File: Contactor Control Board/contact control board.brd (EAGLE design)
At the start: 75.9 x 50.8 mm, 29 parts, among them K1 DS2Y-S-DC5V, Q1 2n2222, Q3 2n2222, Q4 MOSFET-NCHANNELFQP30N06L, U1 LM393AN

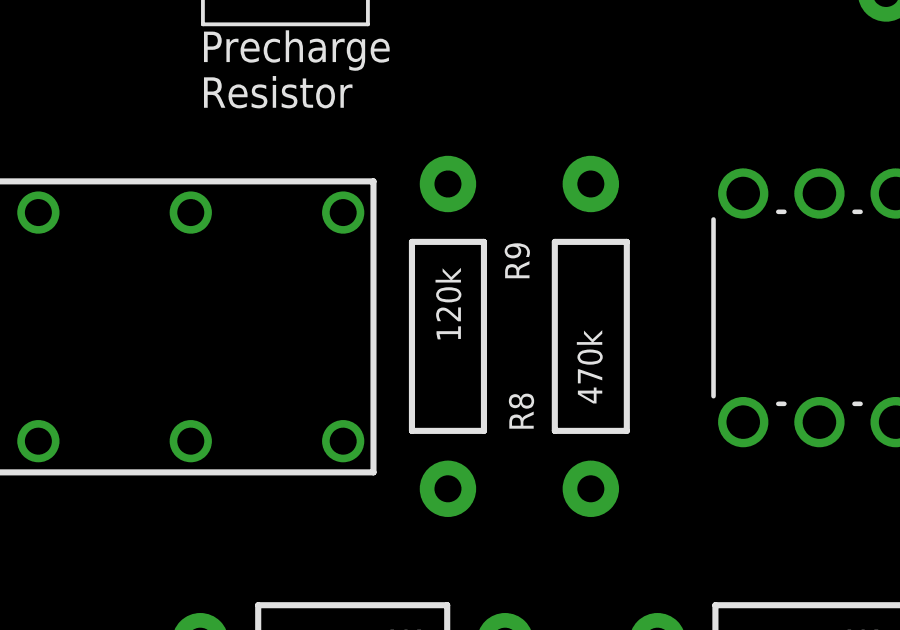
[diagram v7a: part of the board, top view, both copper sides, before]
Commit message: Redoing voltage dividers so that they produce voltages on the oeprational range of our voltage comparator. Also re-wired the voltage
monitor for the capacitors to use capacitor voltage and not the voltage
over the pre-charge resistors.
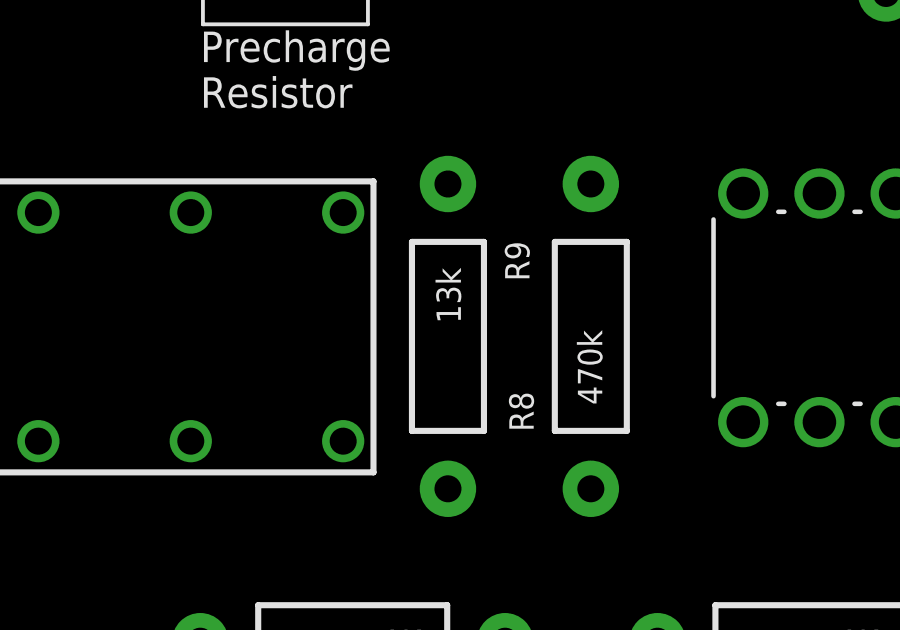
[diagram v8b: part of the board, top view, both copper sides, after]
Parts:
- R9: value 120k -> 13k
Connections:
- net PRECHARGE_OUT: now also R9.P$2
- net PRECHARGE_RESISTOR_IN: no longer R8.P$1
- net PRECHARGE_RESISTOR_OUT: now also R8.P$1; no longer R9.P$2
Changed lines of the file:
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@@
 <setting verticaltext="up"/>
 </settings>
-<grid distance="0.0125" unitdist="inch" unit="inch" style="lines" multiple="1" display="yes" altdistance="0.005" altunitdist="inch" altunit="inch"/>
+<grid distance="0.05" unitdist="inch" unit="inch" style="lines" multiple="1" display="yes" altdistance="0.005" altunitdist="inch" altunit="inch"/>
 <layers>
 <layer number="1" name="Top" color="4" fill="1" visible="yes" active="yes"/>
@@
 <layer number="23" name="tOrigins" color="15" fill="1" visible="yes" active="yes"/>
 <layer number="24" name="bOrigins" color="15" fill="1" visible="yes" active="yes"/>
-<layer number="25" name="tNames" color="16" fill="1" visible="yes" active="yes"/>
+<layer number="25" name="tNames" color="16" fill="1" visible="no" active="yes"/>
 <layer number="26" name="bNames" color="16" fill="1" visible="no" active="yes"/>
 <layer number="27" name="tValues" color="7" fill="1" visible="no" active="yes"/>
@@
 <element name="RESISTOR" library="SparkFun-Connectors" package="1X02_2.54_SCREWTERM" value="M022.54MM_SCREWTERM" x="37.1475" y="46.6725"/>
 <element name="R8" library="SparkFun-Resistors" package="AXIAL-0.4" value="470k" x="48.5775" y="33.02" rot="R90"/>
-<element name="R9" library="SparkFun-Resistors" package="AXIAL-0.4" value="120k" x="43.815" y="33.02" rot="R270"/>
+<element name="R9" library="SparkFun-Resistors" package="AXIAL-0.4" value="13k" x="43.815" y="33.02" rot="R270"/>
 <element name="R10" library="SparkFun-Resistors" package="AXIAL-0.4" value="470k" x="50.165" y="47.625"/>
 <element name="R11" library="SparkFun-Resistors" package="AXIAL-0.4" value="110k" x="63.5" y="47.625"/>
@@
 <contactref element="K1" pad="6"/>
 <contactref element="K1" pad="9"/>
+<contactref element="R9" pad="P$2"/>
 <wire x1="35.2425" y1="29.5275" x2="40.3225" y2="37.1475" width="0" layer="19" extent="1-1"/>
+<wire x1="43.815" y1="27.94" x2="35.2425" y2="29.5275" width="0" layer="19" extent="1-1"/>
 <wire x1="8.5725" y1="30.155" x2="35.2425" y2="29.5275" width="0" layer="19" extent="1-1"/>
 </signal>
@@
 <contactref element="RESISTOR" pad="P1"/>
 <contactref element="K1" pad="4"/>
-<contactref element="R8" pad="P$1"/>
 <wire x1="30.1625" y1="29.5275" x2="39.6875" y2="46.6725" width="0" layer="19" extent="1-1"/>
-<wire x1="48.5775" y1="27.94" x2="30.1625" y2="29.5275" width="0" layer="19" extent="1-1"/>
 </signal>
 <signal name="PRECHARGE_RESISTOR_OUT">
 <contactref element="RESISTOR" pad="P2"/>
 <contactref element="K1" pad="13"/>
-<contactref element="R9" pad="P$2"/>
+<contactref element="R8" pad="P$1"/>
 <wire x1="30.1625" y1="37.1475" x2="37.1475" y2="46.6725" width="0" layer="19" extent="1-1"/>
-<wire x1="43.815" y1="27.94" x2="30.1625" y2="37.1475" width="0" layer="19" extent="1-1"/>
+<wire x1="48.5775" y1="27.94" x2="30.1625" y2="37.1475" width="0" layer="19" extent="1-1"/>
 </signal>
 <signal name="N$2">
